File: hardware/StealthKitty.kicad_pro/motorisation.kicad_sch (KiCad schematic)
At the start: 20 parts, among them J2 Conn_01x06, J3 Conn_01x06, U2 ZXBM5210-S, U3 ZXBM5210-S

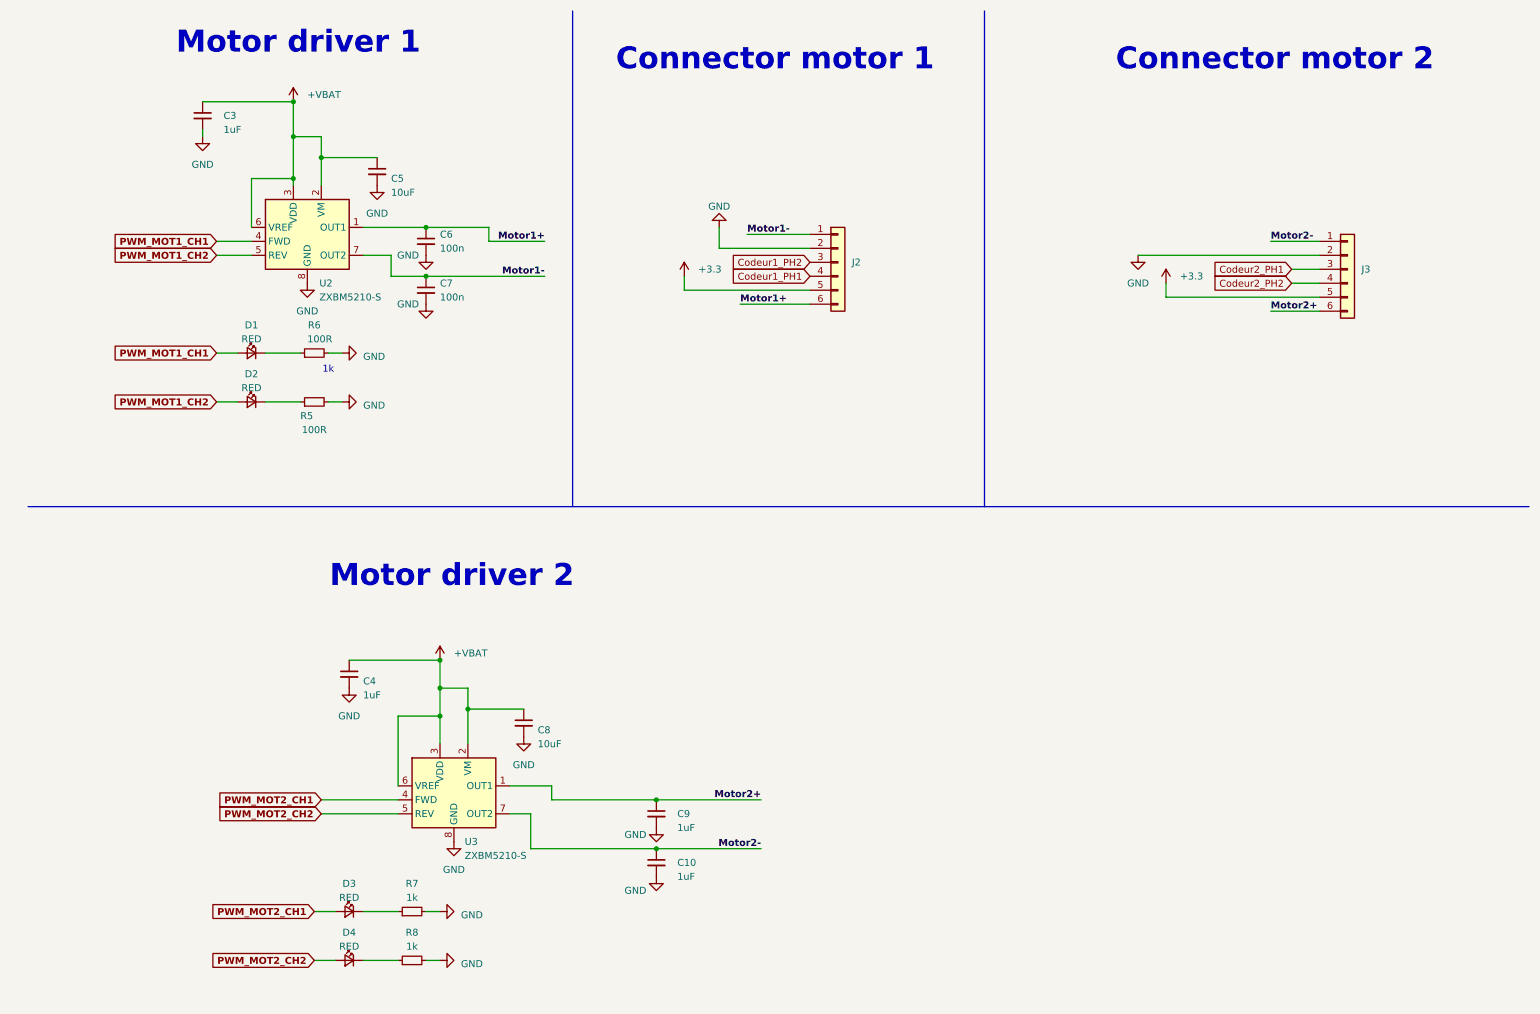
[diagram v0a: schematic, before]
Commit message: réassignation pins stm32, ajout des modifs de la partie power, ajout des modfis de la revue de projet 02/10/24, modifs du 3/10/24 voir readme
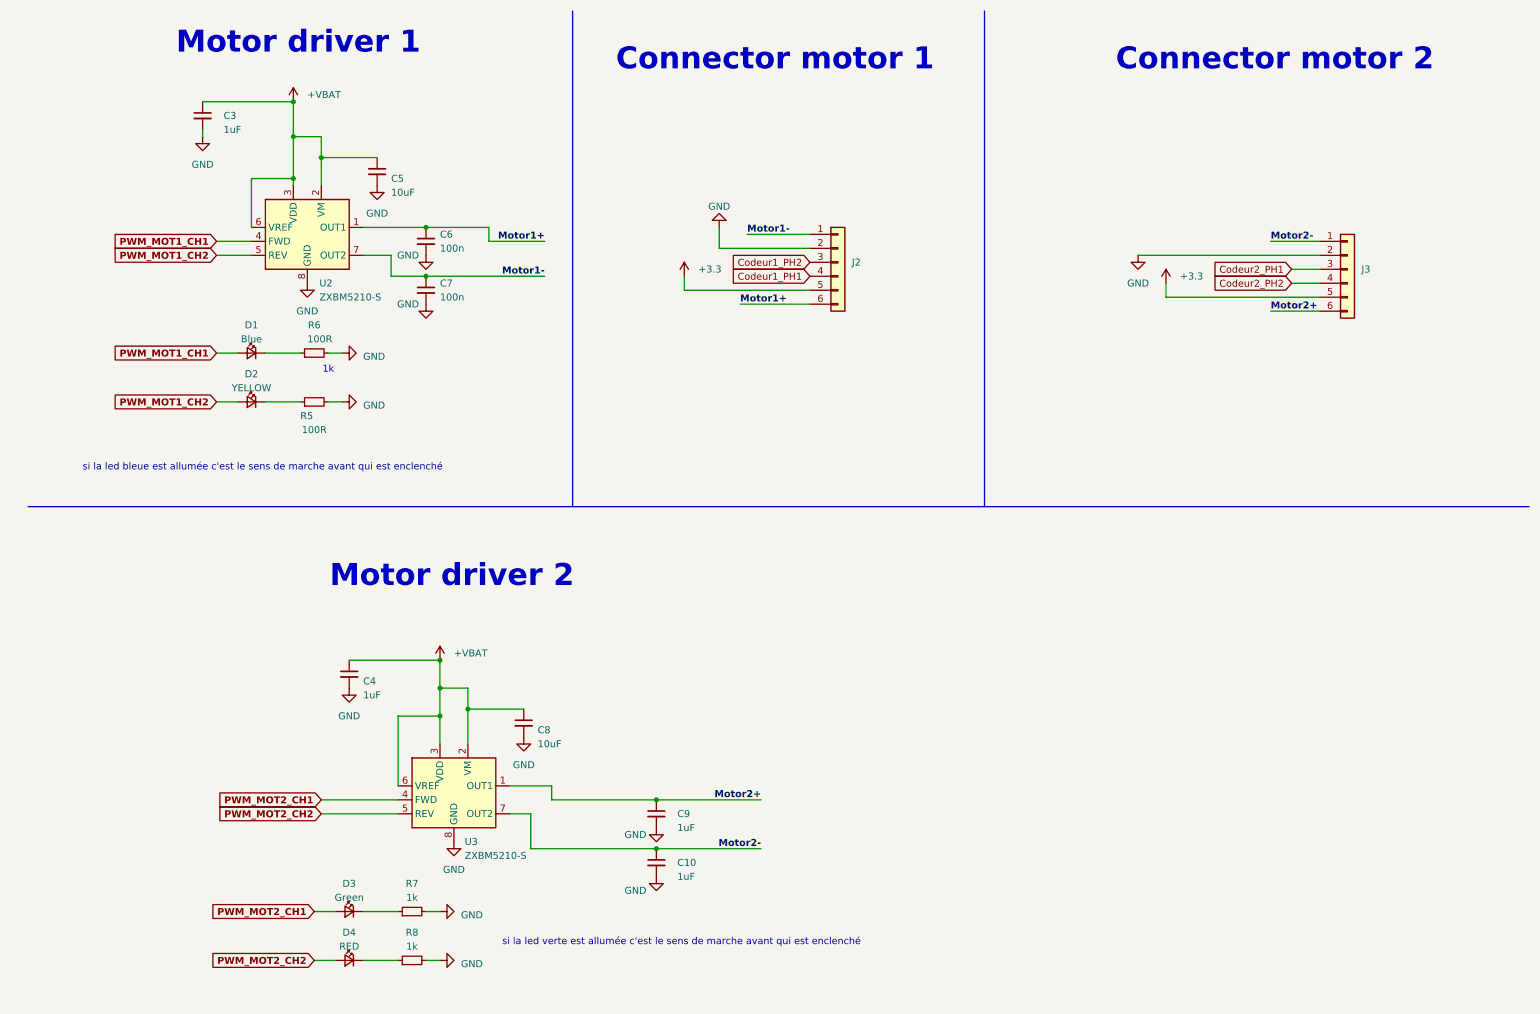
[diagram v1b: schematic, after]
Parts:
- D1: value RED -> Blue
- D2: value RED -> YELLOW
- D3: value RED -> Green
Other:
- note added: "si la led bleue est allumée c'est le sens de marche avant qui est enclenché"
- note added: "si la led verte est allumée c'est le sens de marche avant qui est enclenché"
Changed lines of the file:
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@@
+		)
+	)
+	(text "si la led bleue est allumée c'est le sens de marche avant qui est enclenché"
+		(exclude_from_sim no)
+		(at 55.372 98.298 0)
+		(effects
+			(font
+				(size 1.27 1.27)
+			)
 		)
 	)
@@
 		)
 	)
+	(text "si la led verte est allumée c'est le sens de marche avant qui est enclenché"
+		(exclude_from_sim no)
+		(at 131.572 184.658 0)
+		(effects
+			(font
+				(size 1.27 1.27)
+			)
+		)
+	)
 	(text "Motor driver 2\n"
 		(exclude_from_sim no)
@@
 			)
 		)
-		(property "Value" "RED"
+		(property "Value" "YELLOW"
 			(at 53.34 83.82 0)
 			(effects
@@
 			)
 		)
-		(property "Value" "RED"
+		(property "Value" "Blue"
 			(at 53.34 74.93 0)
 			(effects
@@
 			)
 		)
-		(property "Value" "RED"
+		(property "Value" "Green"
 			(at 71.12 176.53 0)
 			(effects

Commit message: MAJ routage equipe
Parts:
- added TP201: M1_PWM_FWD, TestPoint:TestPoint_Pad_D1.5mm, symbol Connector:TestPoint
- added TP202: M1_PWM_REV, TestPoint:TestPoint_Pad_D1.5mm, symbol Connector:TestPoint
- added TP203: M2_PWM_REV, TestPoint:TestPoint_Pad_D1.5mm, symbol Connector:TestPoint
- added TP204: M2_PWM_FWD, TestPoint:TestPoint_Pad_D1.5mm, symbol Connector:TestPoint
- C6, C7, C8: footprint Capacitor_SMD:C_0603_1608Metric_Pad1.08x0.95mm_HandSolder -> Capacitor_SMD:C_0402_1005Metric_Pad0.74x0.62mm_HandSolder
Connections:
- net PWM_MOT1_CH1: now also TP201.1
- net PWM_MOT1_CH2: now also TP202.1
- net PWM_MOT2_CH1: now also TP204.1
- net PWM_MOT2_CH2: now also TP203.1
- net +3.3 renamed +3.3V

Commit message: Confirmation placement equipe
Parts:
- renumbered C3 to C201, C4 to C202, C5 to C203, C6 to C204, C7 to C205, C8 to C206, C9 to C207, C10 to C208, D1 to D201, D2 to D202, D3 to D203, D4 to D204, J2 to J201, J3 to J202, R5 to R201, R6 to R202, R7 to R203, R8 to R204, TP204 to TP203, TP203 to TP204, U2 to U201, U3 to U202

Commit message: après première revue fiack placement
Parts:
- removed U201, U202: ZXBM5210-S, Package_SO:SOIC-8_3.9x4.9mm_P1.27mm, symbol Driver_Motor:ZXBM5210-S
- added U1, U2: ZXBM5210-SP, Package_SO:Diodes_SO-8EP, symbol Driver_Motor:ZXBM5210-SP
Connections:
- net +VBAT: now also U1.2 (VM), U1.3 (VDD), U1.6 (VREF), U2.2 (VM), U2.3 (VDD), U2.6 (VREF)
- net GND: now also U1.8 (GND), U1.9 (GND), U2.8 (GND), U2.9 (GND)
- net Motor1+: now also U1.1 (OUT1)
- net Motor1-: now also U1.7 (OUT2)
- net Motor2+: now also U2.1 (OUT1)
- net Motor2-: now also U2.7 (OUT2)
- net PWM_MOT1_CH1: now also U1.4 (FWD)
- net PWM_MOT1_CH2: now also U1.5 (REV)
- net PWM_MOT2_CH1: now also U2.4 (FWD)
- net PWM_MOT2_CH2: now also U2.5 (REV)
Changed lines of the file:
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@@
+	)
+	(symbol
+		(lib_id "Driver_Motor:ZXBM5210-SP")
+		(at 90.17 158.75 0)
+		(unit 1)
+		(exclude_from_sim no)
+		(in_bom yes)
+		(on_board yes)
+		(dnp no)
+		(fields_autoplaced yes)
+		(property "Reference" "U2"
+			(at 92.3641 166.37 0)
+			(effects
+				(font
+					(size 1.27 1.27)
+				)
+				(justify left)
+			)
+		)
+		(property "Value" "ZXBM5210-SP"
+			(at 92.3641 168.91 0)
+			(effects
+				(font
+					(size 1.27 1.27)
+				)
+				(justify left)
+			)
+		)
+		(property "Footprint" "Package_SO:Diodes_SO-8EP"
+			(at 91.44 165.1 0)
+			(effects
+				(font
+					(size 1.27 1.27)
+				)
+				(hide yes)
+			)
+		)
+		(property "Datasheet" "https://www.diodes.com/assets/Datasheets/ZXBM5210.pdf"
+			(at 90.17 158.75 0)
+			(effects
+				(font
+					(size 1.27 1.27)
+				)
+				(hide yes)
+			)
+		)
+		(property "Description" "Reversible DC motor drive with speed control, 3-18V, 0.85A, SOIC-8EP"
+			(at 90.17 158.75 0)
+			(effects
+				(font
+					(size 1.27 1.27)
+				)
+				(hide yes)
+			)
+		)
+		(pin "9"
+		)
+		(pin "1"
+		)
+		(pin "3"
+		)
+		(pin "4"
+		)
+		(pin "2"
+		)
+		(pin "8"
+		)
+		(pin "5"
+		)
+		(pin "6"
+		)
+		(pin "7"
+		)
+		(instances
+			(project "StealthKitty.kicad_pro"
+				(path "/23d5732b-7ccb-40aa-85a2-3b18421ac23b/3b52812e-304f-4912-a30c-3c03f9d89b81"
+					(reference "U2")
+					(unit 1)
+				)
+			)
+		)
 	)
 	(symbol
@@
 	)
 	(symbol
-		(lib_id "Driver_Motor:ZXBM5210-S")
-		(at 90.17 158.75 0)
-		(unit 1)
-		(exclude_from_sim no)
-		(in_bom yes)
-		(on_board yes)
-		(dnp no)
-		(fields_autoplaced yes)
-		(property "Reference" "U202"
-			(at 92.1259 166.37 0)
-			(effects
-				(font
-					(size 1.27 1.27)
-				)
-				(justify left)
-			)
-		)
-		(property "Value" "ZXBM5210-S"
-			(at 92.1259 168.91 0)
-			(effects
-				(font
-					(size 1.27 1.27)
-				)
-				(justify left)
-			)
-		)
-		(property "Footprint" "Package_SO:SOIC-8_3.9x4.9mm_P1.27mm"
-			(at 91.44 165.1 0)
-			(effects
-				(font
-					(size 1.27 1.27)
-				)
-				(hide yes)
-			)
-		)
-		(property "Datasheet" "https://www.diodes.com/assets/Datasheets/ZXBM5210.pdf"
-			(at 90.17 158.75 0)
-			(effects
-				(font
-					(size 1.27 1.27)
-				)
-				(hide yes)
-			)
-		)
-		(property "Description" "Reversible DC motor drive with speed control, 3-18V, 0.85A, SOIC-8"
-			(at 90.17 158.75 0)
-			(effects
-				(font
-					(size 1.27 1.27)
-				)
-				(hide yes)
-			)
-		)
-		(property "Mouser Part Number" " 621-ZXBM5210-SP-13 "
-			(at 90.17 158.75 0)
-			(effects
-				(font
-					(size 1.27 1.27)
-				)
-				(hide yes)
-			)
-		)
-		(property "Mouser Price/Stock" "https://www.mouser.fr/ProductDetail/Diodes-Incorporated/ZXBM5210-SP-13?qs=98WN%2FnWUQiQYAgSBGLkvdw%3D%3D"
-			(at 90.17 158.75 0)
-			(effects
-				(font
-					(size 1.27 1.27)
-				)
-				(hide yes)
-			)
-		)
-		(pin "1"
-		)
-		(pin "2"
-		)
-		(pin "3"
-		)
-		(pin "4"
-		)
-		(pin "5"
-		)
-		(pin "6"
-		)
-		(pin "7"
-		)
-		(pin "8"
-		)
-		(instances
-			(project "StealthKitty.kicad_pro"
-				(path "/23d5732b-7ccb-40aa-85a2-3b18421ac23b/3b52812e-304f-4912-a30c-3c03f9d89b81"
-					(reference "U202")
-					(unit 1)
-				)
-			)
-		)
-	)
-	(symbol
 		(lib_id "Device:R_Small")
 		(at 82.55 179.07 90)
@@
 	)
 	(symbol
-		(lib_id "Driver_Motor:ZXBM5210-S")
+		(lib_id "Device:C_Small")
+		(at 102.87 144.78 0)
+		(unit 1)
+		(exclude_from_sim no)
+		(in_bom yes)
+		(on_board yes)
+		(dnp no)
+		(property "Reference" "C206"
+			(at 105.41 146.05 0)
+			(effects
+				(font
+					(size 1.27 1.27)
+				)
+				(justify left)
+			)
+		)
+		(property "Value" "10uF"
+			(at 105.41 148.59 0)
+			(effects
+				(font
+					(size 1.27 1.27)
+				)
+				(justify left)
+			)
+		)
+		(property "Footprint" "Capacitor_SMD:C_0402_1005Metric_Pad0.74x0.62mm_HandSolder"
+			(at 102.87 144.78 0)
+			(effects
+				(font
+					(size 1.27 1.27)
+				)
+				(hide yes)
+			)
+		)
+		(property "Datasheet" "~"
+			(at 102.87 144.78 0)
+			(effects
+				(font
+					(size 1.27 1.27)
+				)
+				(hide yes)
+			)
+		)
+		(property "Description" "Unpolarized capacitor, small symbol"
+			(at 102.87 144.78 0)
+			(effects
+				(font
+					(size 1.27 1.27)
+				)
+				(hide yes)
+			)
+		)
+		(pin "1"
+		)
+		(pin "2"
+		)
+		(instances
+			(project "StealthKitty.kicad_pro"
+				(path "/23d5732b-7ccb-40aa-85a2-3b18421ac23b/3b52812e-304f-4912-a30c-3c03f9d89b81"
+					(reference "C206")
+					(unit 1)
+				)
+			)
+		)
+	)
+	(symbol
+		(lib_id "Driver_Motor:ZXBM5210-SP")
 		(at 63.5 57.15 0)
 		(unit 1)
@@
 		(dnp no)
 		(fields_autoplaced yes)
-		(property "Reference" "U201"
+		(property "Reference" "U1"
 			(at 65.6941 64.77 0)
 			(effects
@@
 			)
 		)
-		(property "Value" "ZXBM5210-S"
+		(property "Value" "ZXBM5210-SP"
 			(at 65.6941 67.31 0)
 			(effects
@@
 			)
 		)
-		(property "Footprint" "Package_SO:SOIC-8_3.9x4.9mm_P1.27mm"
+		(property "Footprint" "Package_SO:Diodes_SO-8EP"
 			(at 64.77 63.5 0)
 			(effects
@@
 			)
 		)
-		(property "Description" "Reversible DC motor drive with speed control, 3-18V, 0.85A, SOIC-8"
+		(property "Description" "Reversible DC motor drive with speed control, 3-18V, 0.85A, SOIC-8EP"
 			(at 63.5 57.15 0)
 			(effects
@@
 			)
 		)
+		(pin "9"
+		)
+		(pin "1"
+		)
+		(pin "3"
+		)
+		(pin "4"
+		)
+		(pin "2"
+		)
+		(pin "8"
+		)
 		(pin "5"
 		)
-		(pin "3"
-		)
 		(pin "6"
 		)
-		(pin "2"
-		)
 		(pin "7"
 		)
-		(pin "8"
-		)
-		(pin "4"
-		)
-		(pin "1"
-		)
-		(instances
-			(project "StealthKitty.kicad_pro"
-				(path "/23d5732b-7ccb-40aa-85a2-3b18421ac23b/3b52812e-304f-4912-a30c-3c03f9d89b81"
-					(reference "U201")
-					(unit 1)
-				)
-			)
-		)
-	)
-	(symbol
-		(lib_id "Device:C_Small")
-		(at 102.87 144.78 0)
-		(unit 1)
-		(exclude_from_sim no)
-		(in_bom yes)
-		(on_board yes)
-		(dnp no)
-		(property "Reference" "C206"
-			(at 105.41 146.05 0)
-			(effects
-				(font
-					(size 1.27 1.27)
-				)
-				(justify left)
-			)
-		)
-		(property "Value" "10uF"
-			(at 105.41 148.59 0)
-			(effects
-				(font
-					(size 1.27 1.27)
-				)
-				(justify left)
-			)
-		)
-		(property "Footprint" "Capacitor_SMD:C_0402_1005Metric_Pad0.74x0.62mm_HandSolder"
-			(at 102.87 144.78 0)
-			(effects
-				(font
-					(size 1.27 1.27)
-				)
-				(hide yes)
-			)
-		)
-		(property "Datasheet" "~"
-			(at 102.87 144.78 0)
-			(effects
-				(font
-					(size 1.27 1.27)
-				)
-				(hide yes)
-			)
-		)
-		(property "Description" "Unpolarized capacitor, small symbol"
-			(at 102.87 144.78 0)
-			(effects
-				(font
-					(size 1.27 1.27)
-				)
-				(hide yes)
-			)
-		)
-		(pin "1"
-		)
-		(pin "2"
-		)
-		(instances
-			(project "StealthKitty.kicad_pro"
-				(path "/23d5732b-7ccb-40aa-85a2-3b18421ac23b/3b52812e-304f-4912-a30c-3c03f9d89b81"
-					(reference "C206")
-					(unit 1)
-				)
+		(instances
+			(project ""
+				(path "/23d5732b-7ccb-40aa-85a2-3b18421ac23b/3b52812e-304f-4912-a30c-3c03f9d89b81"
+					(reference "U1")
+					(unit 1)
+				)

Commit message: Dernier Modif 08/10/2024
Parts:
- removed D201: Blue, LED_SMD:LED_0603_1608Metric_Pad1.05x0.95mm_HandSolder, symbol Device:LED_Small
- removed D202: YELLOW, LED_SMD:LED_0603_1608Metric_Pad1.05x0.95mm_HandSolder, symbol Device:LED_Small
- removed D203: Green, LED_SMD:LED_0603_1608Metric_Pad1.05x0.95mm_HandSolder, symbol Device:LED_Small
- removed D204: RED, LED_SMD:LED_0603_1608Metric_Pad1.05x0.95mm_HandSolder, symbol Device:LED_Small
- removed R201, R202: 100R, Resistor_SMD:R_0603_1608Metric_Pad0.98x0.95mm_HandSolder, symbol Device:R_Small
- removed R203, R204: 1k, Resistor_SMD:R_0603_1608Metric_Pad0.98x0.95mm_HandSolder, symbol Device:R_Small
- C201, C202, C203, C207, C208: footprint Capacitor_SMD:C_0603_1608Metric_Pad1.08x0.95mm_HandSolder -> Capacitor_SMD:C_0402_1005Metric
- C204, C205, C206: footprint Capacitor_SMD:C_0402_1005Metric_Pad0.74x0.62mm_HandSolder -> Capacitor_SMD:C_0402_1005Metric
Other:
- note removed: "1k"
- note removed: "si la led bleue est allumée c'est le sens de marche avant qui est enclenché"
- note removed: "si la led verte est allumée c'est le sens de marche avant qui est enclenché"

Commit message: Modif PCB 16/10/2024 V2
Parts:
- C201, C202, C203, C206, C207, C208: footprint Capacitor_SMD:C_0402_1005Metric -> Capacitor_SMD:C_0603_1608Metric
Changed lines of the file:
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@@
 			)
 		)
-		(property "Footprint" "Capacitor_SMD:C_0402_1005Metric"
+		(property "Footprint" "Capacitor_SMD:C_0603_1608Metric"
 			(at 44.45 34.29 0)
 			(effects
@@
 			)
 		)
-		(property "Footprint" "Capacitor_SMD:C_0402_1005Metric"
+		(property "Footprint" "Capacitor_SMD:C_0603_1608Metric"
 			(at 76.2 44.45 0)
 			(effects
@@
 			)
 		)
-		(property "Footprint" "Capacitor_SMD:C_0402_1005Metric"
+		(property "Footprint" "Capacitor_SMD:C_0603_1608Metric"
 			(at 102.87 144.78 0)
 			(effects
@@
 			)
 		)
-		(property "Footprint" "Capacitor_SMD:C_0402_1005Metric"
+		(property "Footprint" "Capacitor_SMD:C_0603_1608Metric"
 			(at 71.12 135.89 0)
 			(effects
@@
 			)
 		)
-		(property "Footprint" "Capacitor_SMD:C_0402_1005Metric"
+		(property "Footprint" "Capacitor_SMD:C_0603_1608Metric"
 			(at 127 161.29 0)
 			(effects
@@
 			)
 		)
-		(property "Footprint" "Capacitor_SMD:C_0402_1005Metric"
+		(property "Footprint" "Capacitor_SMD:C_0603_1608Metric"
 			(at 127 170.18 0)
 			(effects
